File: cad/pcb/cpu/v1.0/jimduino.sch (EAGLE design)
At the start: 61 parts, among them CN1 SM02B-SRSS-TB, P1 DF12-32-DP, P2 DF12-32-DP, P3 MICROUSB, Q1 FDN360P, Q2 FDN360P, SW1 SWITCH-MOMENTARY-2SMD-REDUNDA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, U1 STM32F415R, U2 MCP1703, U3 MCP73831, U4 LTC2954-2, Y1 16MHz(9pF), Y2 32.768kHz (9pF)

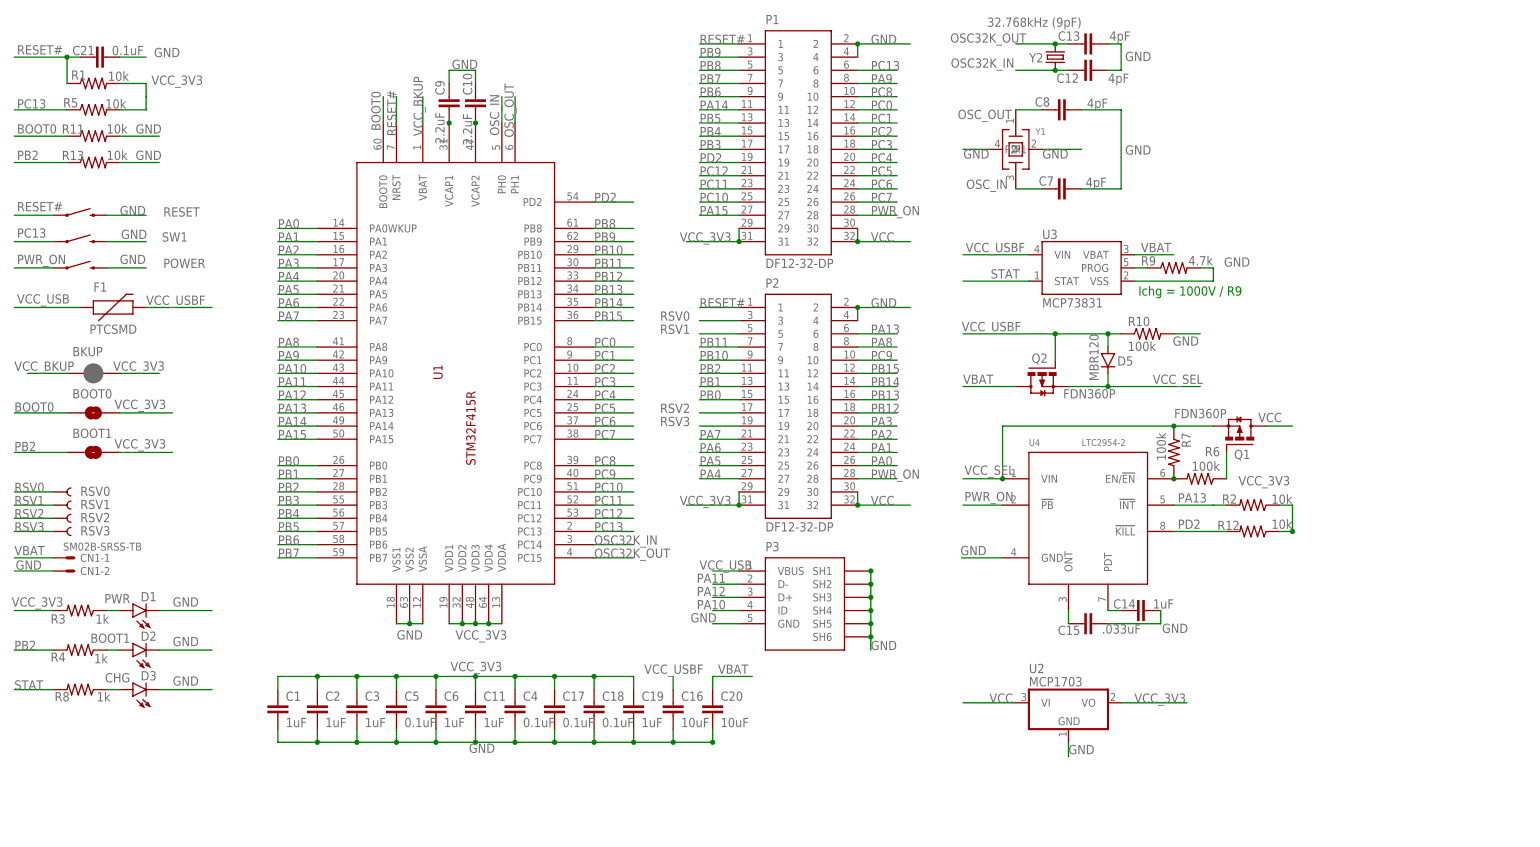
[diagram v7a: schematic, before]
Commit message: New USB connector
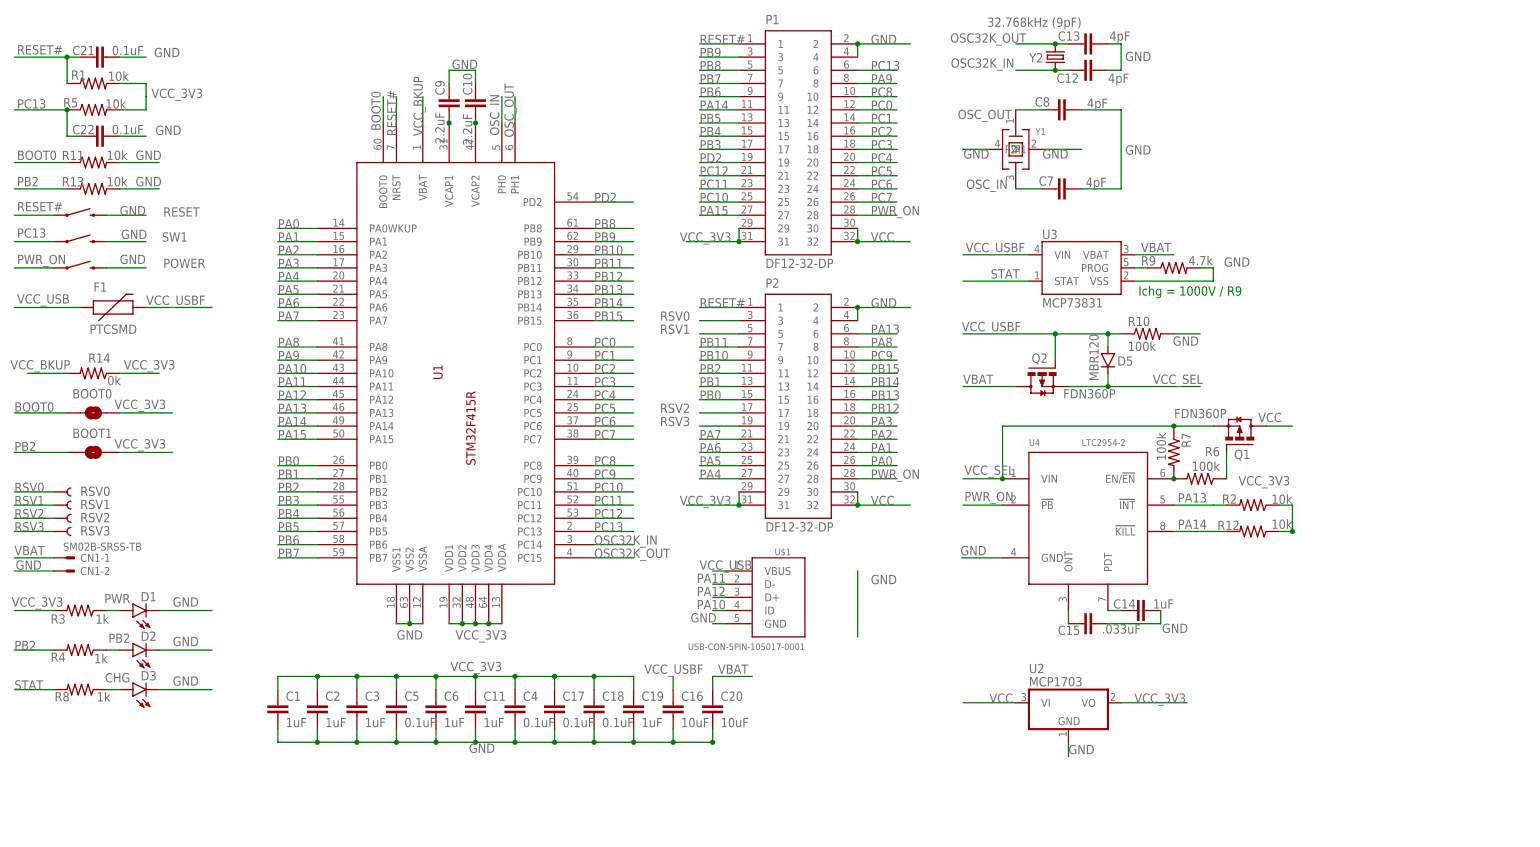
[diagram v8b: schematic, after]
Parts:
- removed BKUP: JUMPER-PAD-2-NC_BY_PASTE, SparkFun-Passives:JUMPER-PAD-2-NC_BY_PASTE
- removed P3: MICROUSB, jimduino:MICROUSB
- added C22: 0.1uF, SparkFun-Capacitors:CAP0805
- added R14: 0k, SparkFun-Passives:RESISTOR0805-RES
- added U$1: USB-CON-5PIN-105017-0001, GeekAmmo:USB-CON-5PIN-105017-0001
- D2: value BOOT1 -> PB2
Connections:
- net GND: now also C22.2, U$1.GND; no longer P3.GND, P3.SH1, P3.SH2, P3.SH3, P3.SH4, P3.SH5, P3.SH6
- net PA10: now also U$1.ID; no longer P3.ID
- net PA11: now also U$1.D-; no longer P3.D-
- net PA12: now also U$1.D+; no longer P3.D+
- net PA14: now also R12.2, U4.!KILL!
- net PC13: now also C22.1
- net PD2: no longer R12.2, U4.!KILL!
- net VCC_3V3: now also R14.1; no longer BKUP.2
- net VCC_BKUP: now also R14.2; no longer BKUP.1
- net VCC_USB: now also U$1.VBUS; no longer P3.VBUS
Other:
- moved on the sheet: R11, R13
